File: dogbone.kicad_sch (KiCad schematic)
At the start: 12 parts, among them M1 THRU_HOLE_PAD, M10 THRU_HOLE_PAD, M11 THRU_HOLE_PAD, M12 THRU_HOLE_PAD, M2 THRU_HOLE_PAD, M3 THRU_HOLE_PAD, M4 THRU_HOLE_PAD, M5 THRU_HOLE_PAD, M6 THRU_HOLE_PAD, M7 THRU_HOLE_PAD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

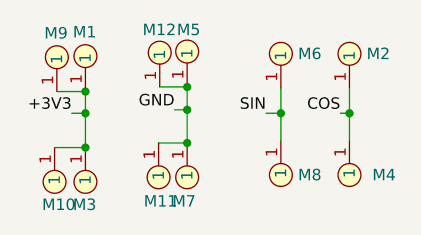
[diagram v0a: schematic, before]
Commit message: net labelling, silkscreen, boards finished
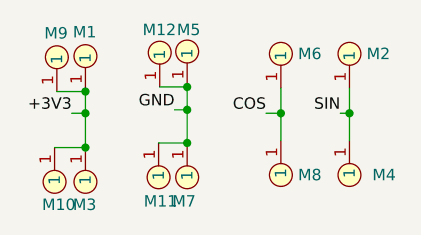
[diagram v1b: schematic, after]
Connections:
- net COS: now also M6.1, M8.1; no longer M2.1, M4.1
- net SIN: now also M2.1, M4.1; no longer M6.1, M8.1
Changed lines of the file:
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@@
     (stroke (width 0) (type default))
-  )
-  (label "SIN" (at 114.554 64.262 180) (fields_autoplaced)
-    (effects (font (size 1.27 1.27)) (justify right bottom))
   )
   (label "GND" (at 104.394 63.881 180) (fields_autoplaced)
     (effects (font (size 1.27 1.27)) (justify right bottom))
   )
-  (label "COS" (at 122.809 64.262 180) (fields_autoplaced)
+  (label "SIN" (at 122.809 64.262 180) (fields_autoplaced)
     (effects (font (size 1.27 1.27)) (justify right bottom))
   )
@@
     (effects (font (size 1.27 1.27)) (justify right bottom))
   )
+  (label "COS" (at 114.554 64.262 180) (fields_autoplaced)
+    (effects (font (size 1.27 1.27)) (justify right bottom))
+  )
